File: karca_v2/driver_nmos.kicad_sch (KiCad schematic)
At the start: 9 parts, among them Q2 IRF3708

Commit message: Version alpha
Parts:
- removed Q2: IRF3708, symbol Simulation_SPICE:NMOS
- added F2: Fuse, Fuse:Fuse_1812_4532Metric, symbol Device:Fuse
- added Q9: IRF3708, IRF3708:TO254P1041X444X1930-3, symbol Simulation_SPICE:NMOS
- R77: renamed from R72; value 910 -> 1k; footprint (none) -> Resistor_SMD:R_1206_3216Metric
- R78: renamed from R73; value 910 -> 1k; footprint (none) -> Resistor_SMD:R_1206_3216Metric
- R79: renamed from R74; footprint (none) -> Resistor_SMD:R_1206_3216Metric
- R80: renamed from R75; footprint (none) -> Resistor_SMD:R_1206_3216Metric
- TP49: renamed from TP37; footprint (none) -> TestPoint:TestPoint_Pad_D2.0mm
- renumbered D32 to D10, D33 to D11, D31 to D9
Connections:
- net +12V: now also F2.1; no longer D10.2 (A), D11.1 (K), D9.2 (A)
- net GND: now also Q9.3 (S)
- net MOS_DRAIN: now also Q9.2 (D)
- net at R79.2, TP49.1: now also Q9.1 (G)
- new net DRV_POS: D10.2 (A), D11.1 (K), D9.2 (A), F2.2

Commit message: discrete traces
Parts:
- renumbered F2 to F3, Q9 to Q4, R77 to R81, R78 to R82, R79 to R83, R80 to R84

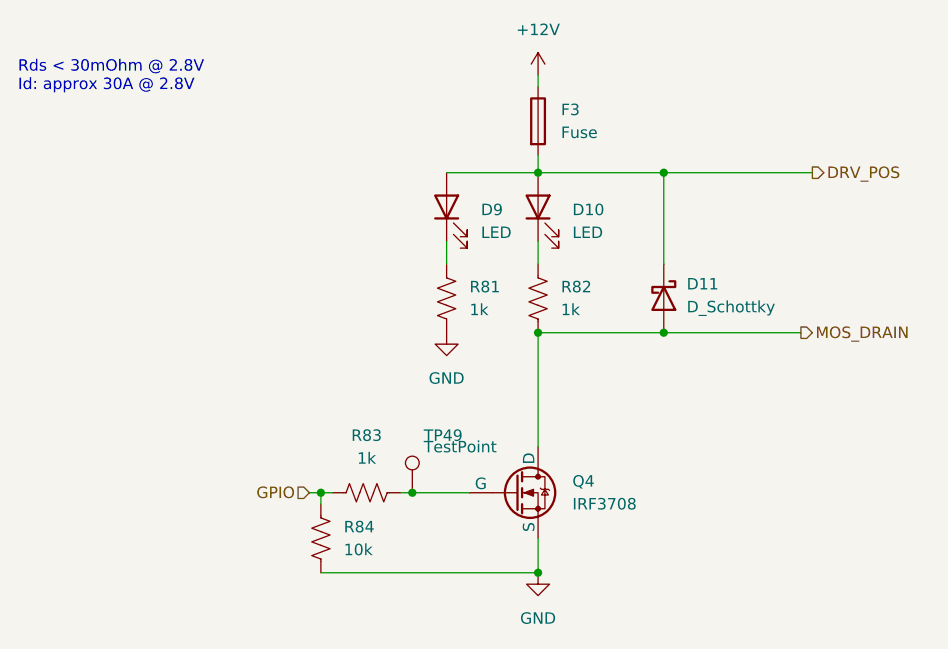
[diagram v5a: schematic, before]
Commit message: Fixed ground capacitors
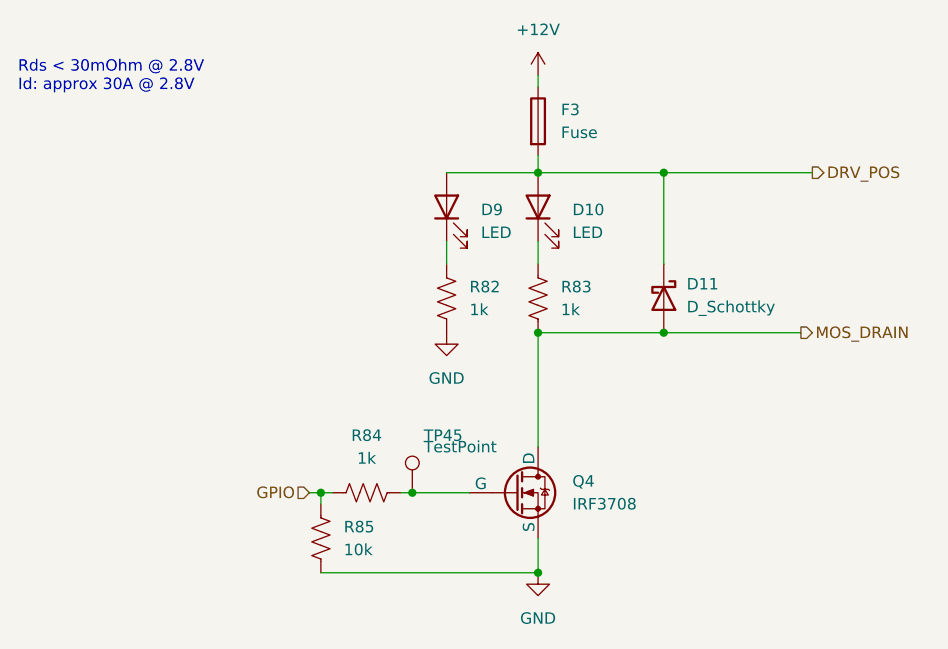
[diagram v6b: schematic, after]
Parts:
- renumbered R81 to R82, R82 to R83, R83 to R84, R84 to R85, TP49 to TP45

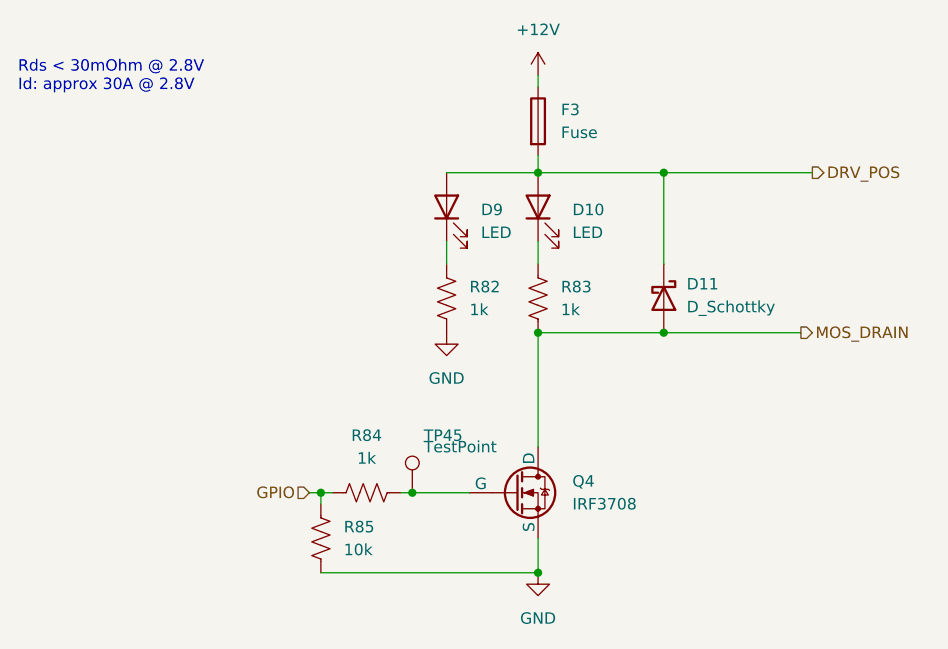
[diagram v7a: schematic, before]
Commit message: cleaned up documentation. Added production files and BOM. Marked Thermocouple components and THT components as DNP (excluded them from BOM too) to match version sent to JLCPCB for fabrication
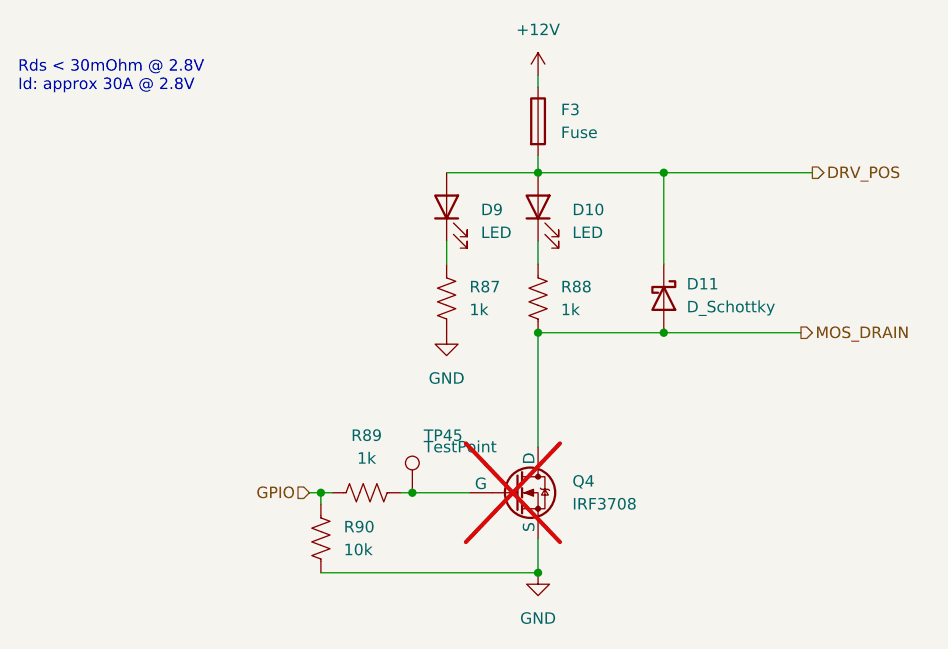
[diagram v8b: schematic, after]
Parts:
- D10: LCSC (none) -> C14641
- D11: LCSC (none) -> C727081
- D9: LCSC (none) -> C125084
- F3: LCSC (none) -> C55996
- Q4: footprint IRF3708:TO254P1041X444X1930-3 -> Package_TO_SOT_THT:TO-220-3_Vertical; now not fitted; now left out of the parts list
- R87: renamed from R82; LCSC (none) -> C104594
- R88: renamed from R83; LCSC (none) -> C104594
- R89: renamed from R84; LCSC (none) -> C104594
- R90: renamed from R85; LCSC (none) -> C1489
- TP45: now left out of the parts list
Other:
- company: (none) -> Rice Eclipse
- title: (none) -> kARCA 2.0 Engine Control System
